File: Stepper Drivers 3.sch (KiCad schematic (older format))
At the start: 22 parts

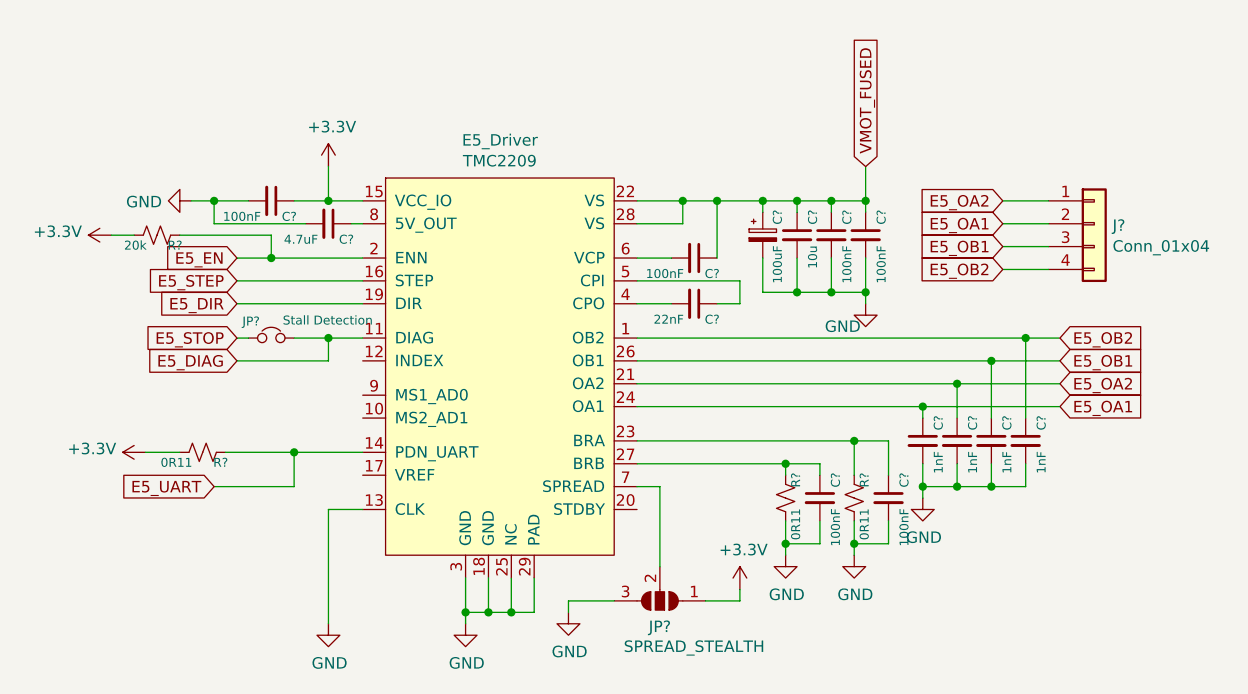
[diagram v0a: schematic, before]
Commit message: added resistor numbers
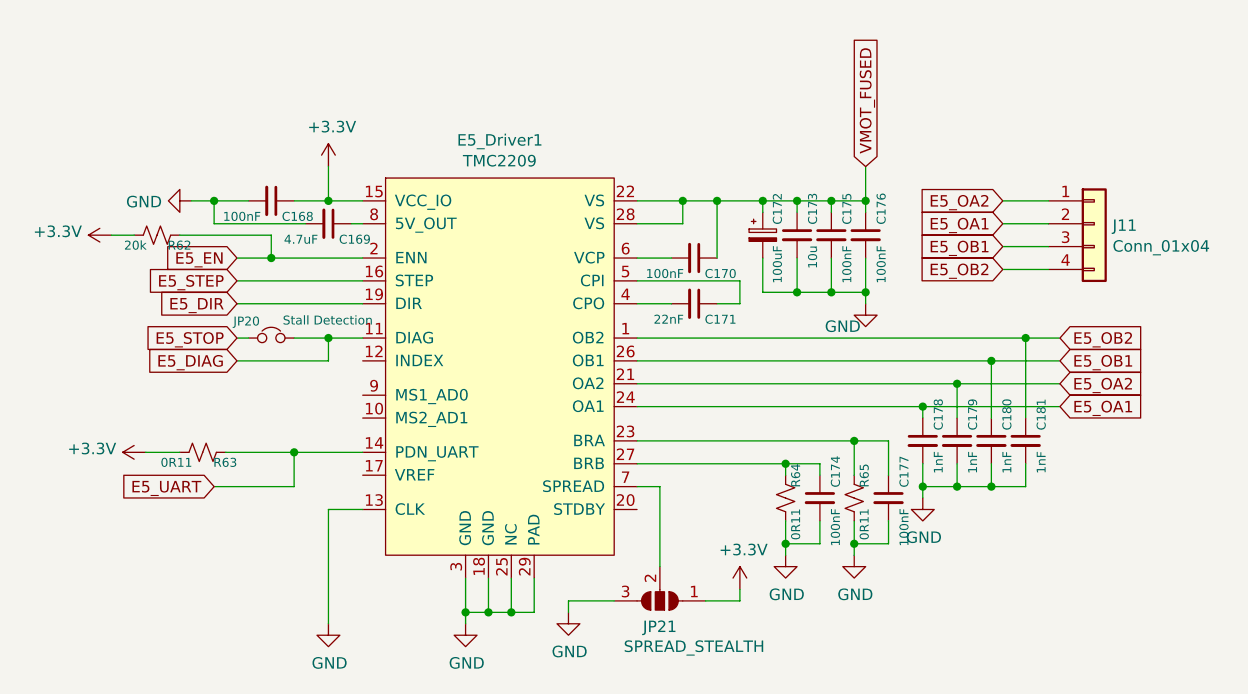
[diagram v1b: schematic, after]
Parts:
- gave numbers to parts that had none: 21
- renumbered E5_Driver to E5_Driver1

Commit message: added raspberry pi header
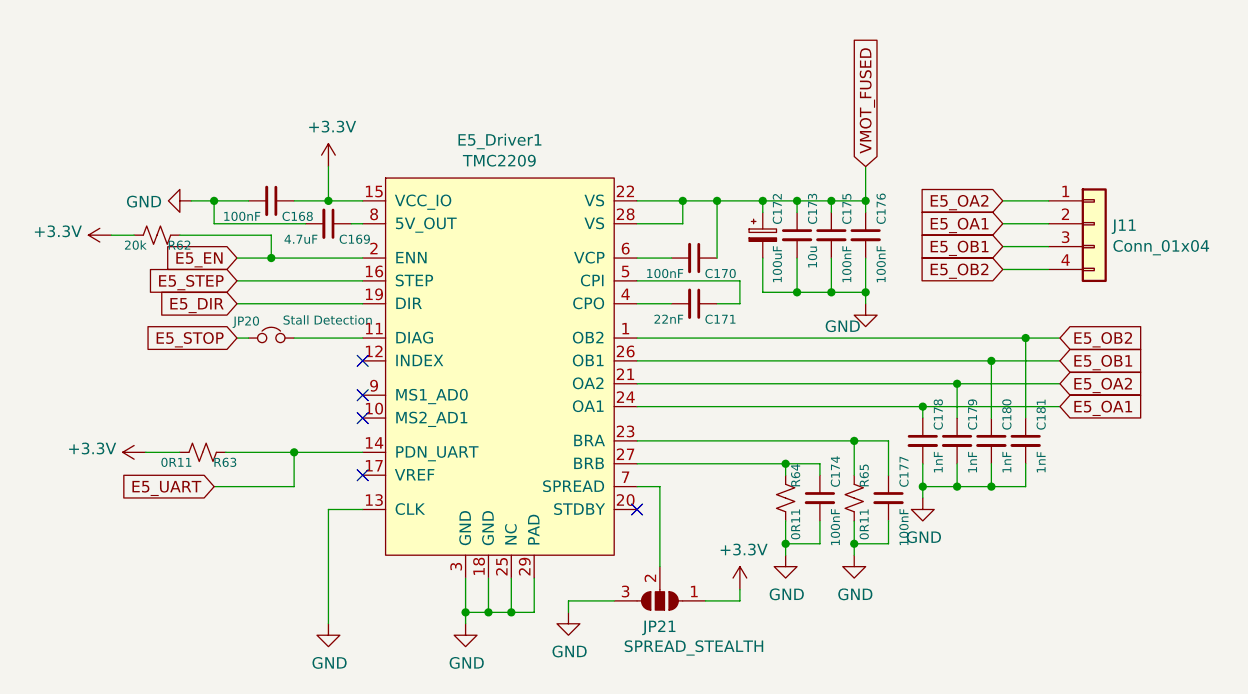
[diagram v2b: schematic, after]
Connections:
- net E5_DIAG: no longer names the net of E5_Driver1.11 (DIAG), JP20.2
- no-connect marks 0 -> 5
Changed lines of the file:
@@
 $EndComp
-Wire Wire Line
-	4250 3600 4650 3600
-Wire Wire Line
-	4650 3600 4650 3500
-Wire Wire Line
-	4650 3500 4800 3500
 Wire Wire Line
 	4250 3500 4300 3500
-Wire Wire Line
-	4500 3500 4650 3500
-Connection ~ 4650 3500
 $Comp
 L Device:C_Small C?
@@
 Text GLabel 4250 3500 0    50   Input ~ 0
 E5_STOP
-Text GLabel 4250 3600 0    50   Input ~ 0
-E5_DIAG
 Text GLabel 4150 4150 0    50   Input ~ 0
 E5_UART
+NoConn ~ 4800 3600
+NoConn ~ 4800 3750
+NoConn ~ 4800 3850
+NoConn ~ 4800 4100
+NoConn ~ 6000 4250
+Wire Wire Line
+	4500 3500 4800 3500
 $EndSCHEMATC

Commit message: assigned some footprints
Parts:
- C168, C170, C174, C175, C176, C177: footprint (none) -> Capacitor_SMD:C_0603_1608Metric_Pad1.05x0.95mm_HandSolder
- C172: footprint (none) -> Capacitor_SMD:CP_Elec_6.3x7.7
- C173: footprint (none) -> Capacitor_SMD:C_0805_2012Metric_Pad1.15x1.40mm_HandSolder
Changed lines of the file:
@@
 F 0 "C172" V 6638 3096 39  0000 L BNN
 F 1 "100uF" V 6638 3005 39  0000 R BNN
-F 2 "" H 6550 3050 50  0001 C CNN
+F 2 "Capacitor_SMD:CP_Elec_6.3x7.7" H 6550 3050 50  0001 C CNN
 F 3 "~" H 6550 3050 50  0001 C CNN
 	1    6550 3050
@@
 F 0 "C173" V 6792 3096 39  0000 L BNN
 F 1 "10u" V 6792 3005 39  0000 R BNN
-F 2 "" H 6700 3050 50  0001 C CNN
+F 2 "Capacitor_SMD:C_0805_2012Metric_Pad1.15x1.40mm_HandSolder" H 6700 3050 50  0001 C CNN
 F 3 "~" H 6700 3050 50  0001 C CNN
 	1    6700 3050
@@
 F 0 "C176" V 7092 3096 39  0000 L BNN
 F 1 "100nF" V 7092 3005 39  0000 R BNN
-F 2 "" H 7000 3050 50  0001 C CNN
+F 2 "Capacitor_SMD:C_0603_1608Metric_Pad1.05x0.95mm_HandSolder" H 7000 3050 50  0001 C CNN
 F 3 "~" H 7000 3050 50  0001 C CNN
 	1    7000 3050
@@
 F 0 "C175" V 6942 3096 39  0000 L BNN
 F 1 "100nF" V 6942 3005 39  0000 R BNN
-F 2 "" H 6850 3050 50  0001 C CNN
+F 2 "Capacitor_SMD:C_0603_1608Metric_Pad1.05x0.95mm_HandSolder" H 6850 3050 50  0001 C CNN
 F 3 "~" H 6850 3050 50  0001 C CNN
 	1    6850 3050
@@
 F 0 "C170" V 6342 3196 39  0000 L BNN
 F 1 "100nF" V 6342 3105 39  0000 R BNN
-F 2 "" H 6250 3150 50  0001 C CNN
+F 2 "Capacitor_SMD:C_0603_1608Metric_Pad1.05x0.95mm_HandSolder" H 6250 3150 50  0001 C CNN
 F 3 "~" H 6250 3150 50  0001 C CNN
 	1    6250 3150
@@
 F 0 "C168" V 4492 2946 39  0000 L BNN
 F 1 "100nF" V 4492 2855 39  0000 R BNN
-F 2 "" H 4400 2900 50  0001 C CNN
+F 2 "Capacitor_SMD:C_0603_1608Metric_Pad1.05x0.95mm_HandSolder" H 4400 2900 50  0001 C CNN
 F 3 "~" H 4400 2900 50  0001 C CNN
 	1    4400 2900
@@
 F 0 "C177" V 7192 4246 39  0000 L BNN
 F 1 "100nF" V 7192 4155 39  0000 R BNN
-F 2 "" H 7100 4200 50  0001 C CNN
+F 2 "Capacitor_SMD:C_0603_1608Metric_Pad1.05x0.95mm_HandSolder" H 7100 4200 50  0001 C CNN
 F 3 "~" H 7100 4200 50  0001 C CNN
 	1    7100 4200
@@
 F 0 "C174" V 6892 4246 39  0000 L BNN
 F 1 "100nF" V 6892 4155 39  0000 R BNN
-F 2 "" H 6800 4200 50  0001 C CNN
+F 2 "Capacitor_SMD:C_0603_1608Metric_Pad1.05x0.95mm_HandSolder" H 6800 4200 50  0001 C CNN
 F 3 "~" H 6800 4200 50  0001 C CNN
 	1    6800 4200

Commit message: associated more footprints
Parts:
- C169: footprint (none) -> Capacitor_SMD:C_0805_2012Metric_Pad1.15x1.40mm_HandSolder
- C171, C178, C179, C180, C181: footprint (none) -> Capacitor_SMD:C_0603_1608Metric_Pad1.05x0.95mm_HandSolder
- J11: footprint (none) -> Connector_Molex:Molex_KK-254_AE-6410-04A_1x04_P2.54mm_Vertical
- JP20: footprint (none) -> Connector_PinHeader_2.54mm:PinHeader_1x02_P2.54mm_Vertical
- JP21: footprint (none) -> Connector_PinHeader_2.54mm:PinHeader_1x03_P2.54mm_Vertical
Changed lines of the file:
@@
 F 0 "C171" V 6342 3396 39  0000 L BNN
 F 1 "22nF" V 6342 3305 39  0000 R BNN
-F 2 "" H 6250 3350 50  0001 C CNN
+F 2 "Capacitor_SMD:C_0603_1608Metric_Pad1.05x0.95mm_HandSolder" H 6250 3350 50  0001 C CNN
 F 3 "~" H 6250 3350 50  0001 C CNN
 	1    6250 3350
@@
 F 0 "C169" V 4742 3046 39  0000 L BNN
 F 1 "4.7uF" V 4742 2955 39  0000 R BNN
-F 2 "" H 4650 3000 50  0001 C CNN
+F 2 "Capacitor_SMD:C_0805_2012Metric_Pad1.15x1.40mm_HandSolder" H 4650 3000 50  0001 C CNN
 F 3 "~" H 4650 3000 50  0001 C CNN
 	1    4650 3000
@@
 F 0 "JP20" H 4350 3550 39  0000 R BNN
 F 1 "Stall Detection" H 4450 3600 39  0000 L TNN
-F 2 "" H 4400 3500 50  0001 C CNN
+F 2 "Connector_PinHeader_2.54mm:PinHeader_1x02_P2.54mm_Vertical" H 4400 3500 50  0001 C CNN
 F 3 "~" H 4400 3500 50  0001 C CNN
 	1    4400 3500
@@
 F 0 "C178" V 7342 3996 39  0000 L BNN
 F 1 "1nF" V 7342 3905 39  0000 R BNN
-F 2 "" H 7250 3950 50  0001 C CNN
+F 2 "Capacitor_SMD:C_0603_1608Metric_Pad1.05x0.95mm_HandSolder" H 7250 3950 50  0001 C CNN
 F 3 "~" H 7250 3950 50  0001 C CNN
 	1    7250 3950
@@
 F 0 "C179" V 7492 3996 39  0000 L BNN
 F 1 "1nF" V 7492 3905 39  0000 R BNN
-F 2 "" H 7400 3950 50  0001 C CNN
+F 2 "Capacitor_SMD:C_0603_1608Metric_Pad1.05x0.95mm_HandSolder" H 7400 3950 50  0001 C CNN
 F 3 "~" H 7400 3950 50  0001 C CNN
 	1    7400 3950
@@
 F 0 "C180" V 7642 3996 39  0000 L BNN
 F 1 "1nF" V 7642 3905 39  0000 R BNN
-F 2 "" H 7550 3950 50  0001 C CNN
+F 2 "Capacitor_SMD:C_0603_1608Metric_Pad1.05x0.95mm_HandSolder" H 7550 3950 50  0001 C CNN
 F 3 "~" H 7550 3950 50  0001 C CNN
 	1    7550 3950
@@
 F 0 "C181" V 7792 3996 39  0000 L BNN
 F 1 "1nF" V 7792 3905 39  0000 R BNN
-F 2 "" H 7700 3950 50  0001 C CNN
+F 2 "Capacitor_SMD:C_0603_1608Metric_Pad1.05x0.95mm_HandSolder" H 7700 3950 50  0001 C CNN
 F 3 "~" H 7700 3950 50  0001 C CNN
 	1    7700 3950
@@
 F 0 "J11" H 8080 2992 50  0000 L CNN
 F 1 "Conn_01x04" H 8080 2901 50  0000 L CNN
-F 2 "" H 8000 3000 50  0001 C CNN
+F 2 "Connector_Molex:Molex_KK-254_AE-6410-04A_1x04_P2.54mm_Vertical" H 8000 3000 50  0001 C CNN
 F 3 "~" H 8000 3000 50  0001 C CNN
 	1    8000 3000
@@
 F 0 "JP21" H 6100 4763 50  0000 C CNN
 F 1 "SPREAD_STEALTH" H 5950 4850 50  0000 C CNN
-F 2 "" H 6100 4650 50  0001 C CNN
+F 2 "Connector_PinHeader_2.54mm:PinHeader_1x03_P2.54mm_Vertical" H 6100 4650 50  0001 C CNN
 F 3 "~" H 6100 4650 50  0001 C CNN
 	1    6100 4650

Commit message: Added more footprints
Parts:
- E5_Driver1: footprint (none) -> Package_DFN_QFN:QFN-28-1EP_5x5mm_P0.5mm_EP3.35x3.35mm_ThermalVias
- R62: footprint (none) -> Resistor_SMD:R_0603_1608Metric_Pad1.05x0.95mm_HandSolder
- R63, R64, R65: footprint (none) -> Resistor_SMD:R_0805_2012Metric_Pad1.15x1.40mm_HandSolder
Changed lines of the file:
@@
 $Descr A4 11693 8268
 encoding utf-8
-Sheet 9 9
+Sheet 7 9
 Title ""
 Date ""
@@
 F 0 "R64" V 6718 4246 39  0000 L BNN
 F 1 "0R11" V 6718 4155 39  0000 R BNN
-F 2 "" H 6650 4200 50  0001 C CNN
+F 2 "Resistor_SMD:R_0805_2012Metric_Pad1.15x1.40mm_HandSolder" H 6650 4200 50  0001 C CNN
 F 3 "~" H 6650 4200 50  0001 C CNN
 	1    6650 4200
@@
 F 0 "R65" V 7018 4246 39  0000 L BNN
 F 1 "0R11" V 7018 4155 39  0000 R BNN
-F 2 "" H 6950 4200 50  0001 C CNN
+F 2 "Resistor_SMD:R_0805_2012Metric_Pad1.15x1.40mm_HandSolder" H 6950 4200 50  0001 C CNN
 F 3 "~" H 6950 4200 50  0001 C CNN
 	1    6950 4200
@@
 F 0 "R63" V 4168 4046 39  0000 L BNN
 F 1 "0R11" V 4168 3955 39  0000 R BNN
-F 2 "" H 4100 4000 50  0001 C CNN
+F 2 "Resistor_SMD:R_0805_2012Metric_Pad1.15x1.40mm_HandSolder" H 4100 4000 50  0001 C CNN
 F 3 "~" H 4100 4000 50  0001 C CNN
 	1    4100 4000
@@
 F 0 "R62" V 3968 3096 39  0000 L BNN
 F 1 "20k" V 3968 3005 39  0000 R BNN
-F 2 "" H 3900 3050 50  0001 C CNN
+F 2 "Resistor_SMD:R_0603_1608Metric_Pad1.05x0.95mm_HandSolder" H 3900 3050 50  0001 C CNN
 F 3 "~" H 3900 3050 50  0001 C CNN
 	1    3900 3050
@@
 F 0 "E5_Driver1" H 5400 4265 50  0000 C CNN
 F 1 "TMC2209" H 5400 4174 50  0000 C CNN
-F 2 "" H 5500 3450 50  0001 C CNN
+F 2 "Package_DFN_QFN:QFN-28-1EP_5x5mm_P0.5mm_EP3.35x3.35mm_ThermalVias" H 5500 3450 50  0001 C CNN
 F 3 "" H 5500 3450 50  0001 C CNN
 	1    5400 3450

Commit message: started some routing
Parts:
- JP21: footprint Connector_PinHeader_2.54mm:PinHeader_1x03_P2.54mm_Vertical -> Jumper:SolderJumper-3_P1.3mm_Open_RoundedPad1.0x1.5mm
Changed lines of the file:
@@
 F 0 "JP21" H 6100 4763 50  0000 C CNN
 F 1 "SPREAD_STEALTH" H 5950 4850 50  0000 C CNN
-F 2 "Connector_PinHeader_2.54mm:PinHeader_1x03_P2.54mm_Vertical" H 6100 4650 50  0001 C CNN
+F 2 "Jumper:SolderJumper-3_P1.3mm_Open_RoundedPad1.0x1.5mm" H 6100 4650 50  0001 C CNN
 F 3 "~" H 6100 4650 50  0001 C CNN
 	1    6100 4650
